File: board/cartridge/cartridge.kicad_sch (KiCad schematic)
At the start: 33 parts, among them J1 TF-115-BCP9, J2 HC-TYPE-C-16P-01B, J3 TC2030-NL, P1 Card Edge, SW1 K3-1410S, SW2 K3-1410S, U1 STM32G0B0RETx, U2 NAU8814Y, U3 AMS1117-3.3, Y1 X322516MLB4SI

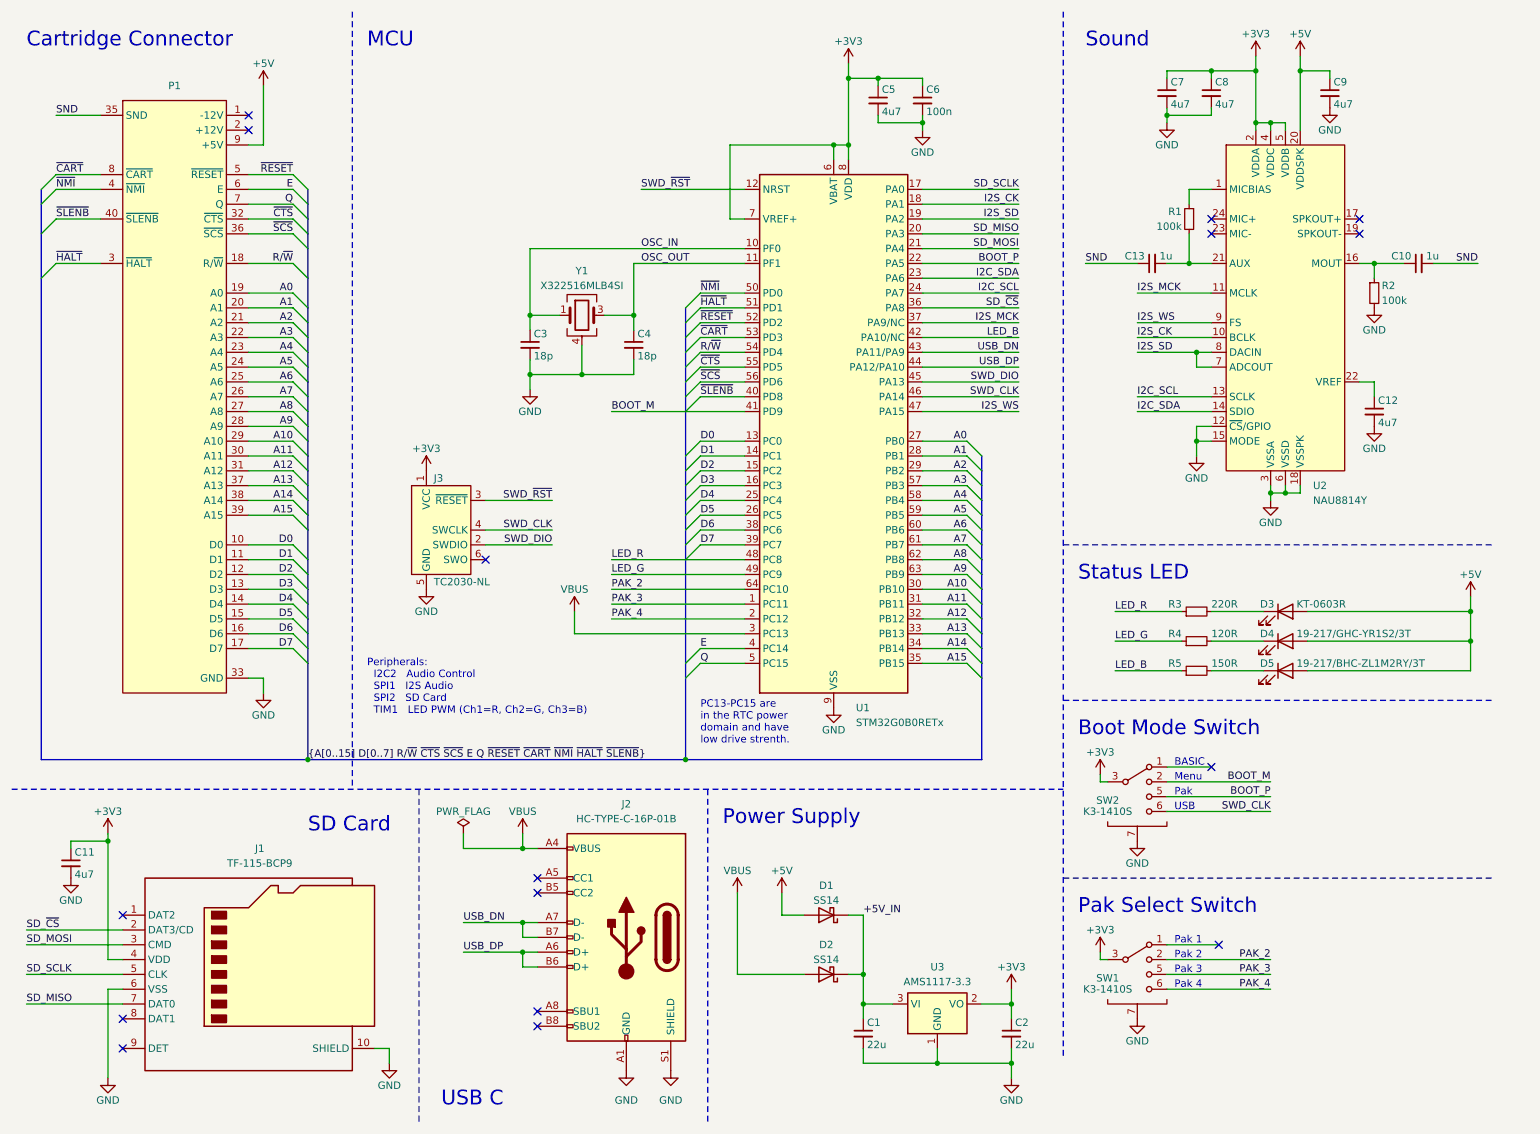
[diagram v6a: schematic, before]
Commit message: Update KiCad projects to v8.
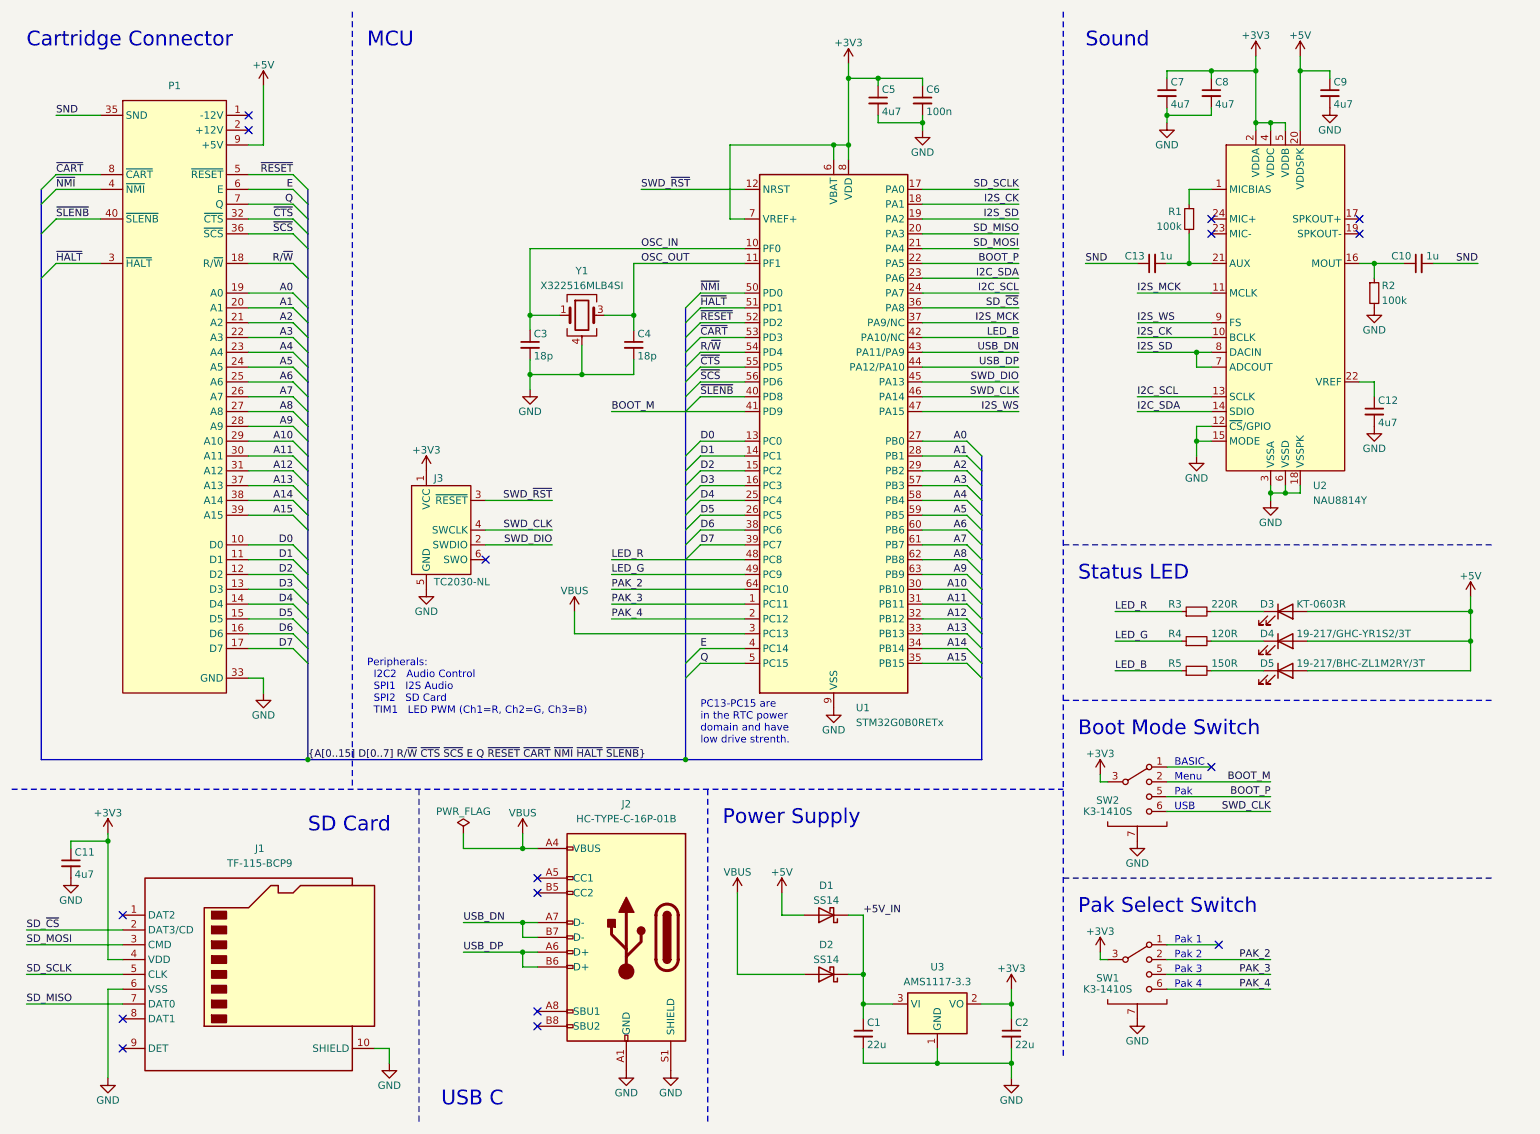
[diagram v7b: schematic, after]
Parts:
- J2: symbol Connector:USB_C_Receptacle_USB2.0 -> Connector:USB_C_Receptacle_USB2.0_16P

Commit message: Sketch out a redesign to use an RP2040.
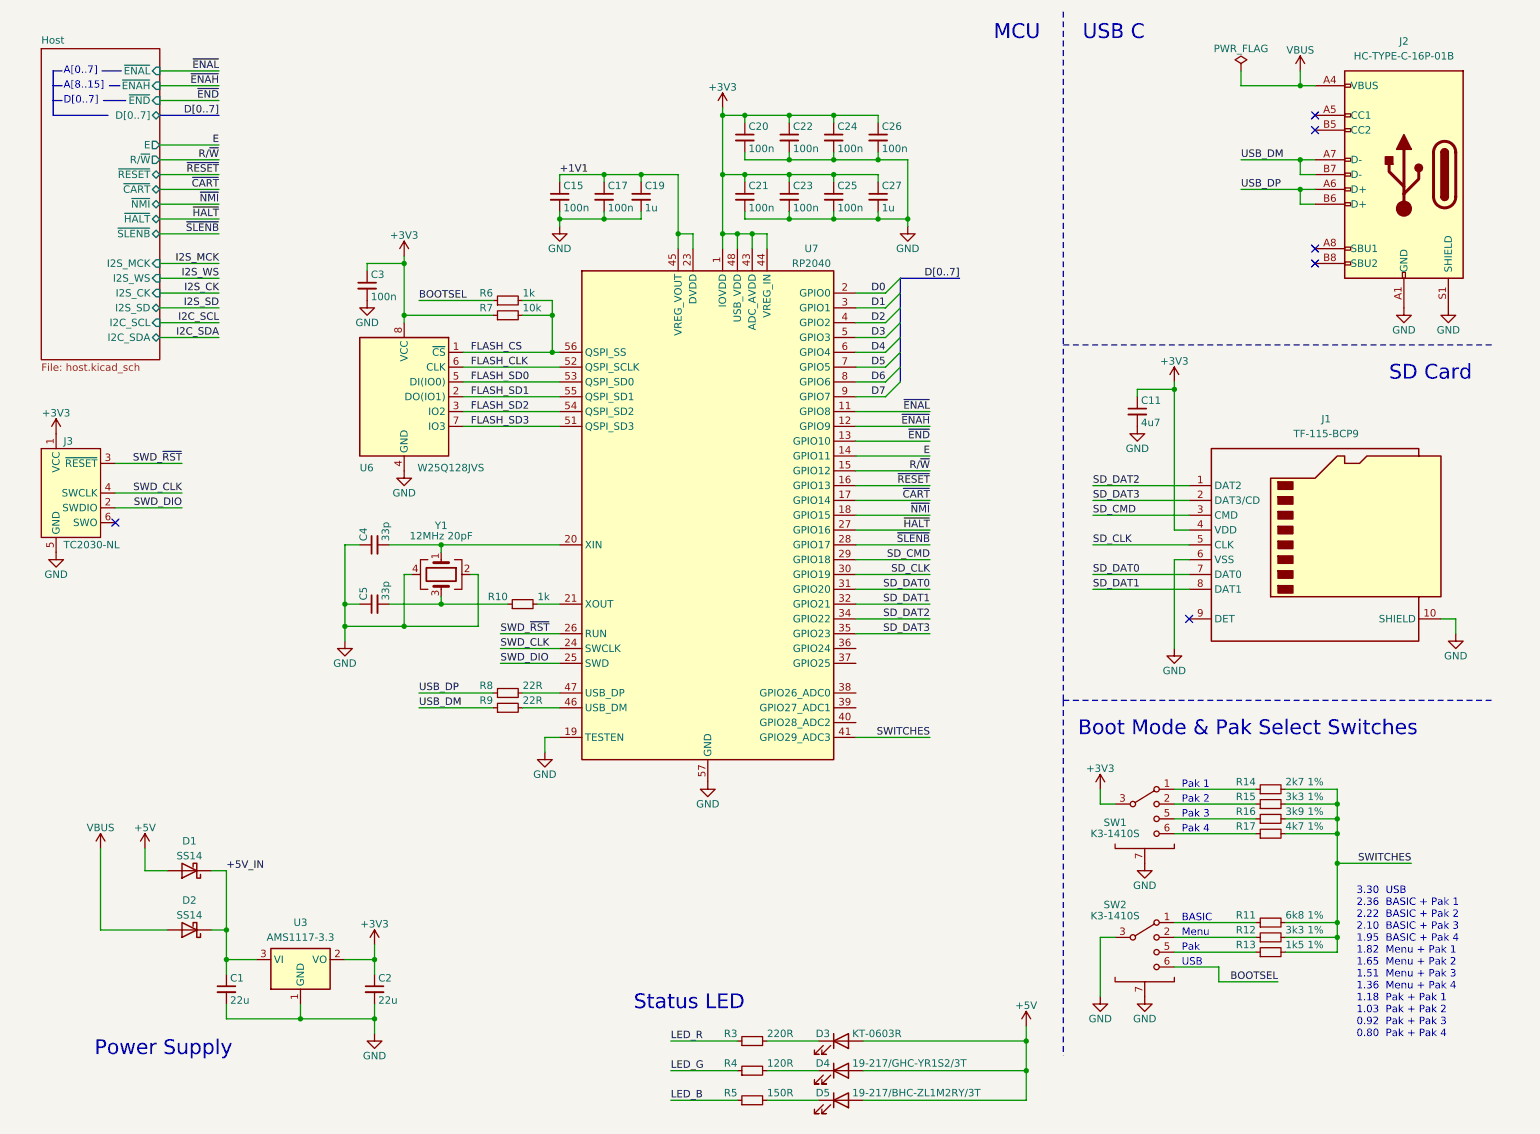
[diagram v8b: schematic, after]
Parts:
- removed C10, C13: 1u, Capacitor_SMD:C_0603_1608Metric, symbol Device:C_Small
- removed C12, C7, C8, C9: 4u7, Capacitor_SMD:C_0603_1608Metric, symbol Device:C_Small
- removed C6: 100n, Capacitor_SMD:C_0603_1608Metric, symbol Device:C_Small
- removed P1: Card Edge, 0Project:CoCo_Cart, symbol 0Project:CoCo_Cart
- removed R1, R2: 100k, Resistor_SMD:R_0603_1608Metric, symbol Device:R_Small
- removed U1: STM32G0B0RETx, Package_QFP:LQFP-64_10x10mm_P0.5mm, symbol MCU_ST_STM32G0:STM32G0B0RETx
- removed U2: NAU8814Y, Package_DFN_QFN:VQFN-24-1EP_4x4mm_P0.5mm_EP2.5x2.5mm, symbol 0Project:Nuvoton_NAU8814Y
- added C15, C17, C20, C21, C22, C23, C24, C25, C26: 100n, Capacitor_SMD:C_0603_1608Metric, symbol Device:C_Small
- added C19, C27: 1u, Capacitor_SMD:C_0603_1608Metric, symbol Device:C_Small
- added R10, R6: 1k, Resistor_SMD:R_0603_1608Metric, symbol Device:R_Small
- added R11: 6k8 1%, Resistor_SMD:R_0603_1608Metric, symbol Device:R_Small
- added R12, R15: 3k3 1%, Resistor_SMD:R_0603_1608Metric, symbol Device:R_Small
- added R13: 1k5 1%, Resistor_SMD:R_0603_1608Metric, symbol Device:R_Small
- added R14: 2k7 1%, Resistor_SMD:R_0603_1608Metric, symbol Device:R_Small
- added R16: 3k9 1%, Resistor_SMD:R_0603_1608Metric, symbol Device:R_Small
- added R17: 4k7 1%, Resistor_SMD:R_0603_1608Metric, symbol Device:R_Small
- added R7: 10k, Resistor_SMD:R_0603_1608Metric, symbol Device:R_Small
- added R8, R9: 22R, Resistor_SMD:R_0603_1608Metric, symbol Device:R_Small
- added U6: W25Q128JVS, Package_SO:SOIC-8_5.23x5.23mm_P1.27mm, symbol Memory_Flash:W25Q128JVS
- added U7: RP2040, Package_DFN_QFN:QFN-56-1EP_7x7mm_P0.4mm_EP3.2x3.2mm, symbol 0Project:RP2040
- C3: value 18p -> 100n
- C4: value 18p -> 33p
- C5: value 4u7 -> 33p
- Y1: value X322516MLB4SI -> 12MHz 20pF; LCSC C13738 -> C9002
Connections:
- net +3V3: now also C3.1, C20.1, C21.1, C22.1, C23.1, C24.1, C25.1, C26.1, C27.1, R7.1, U6.8 (VCC), U7.1 (IOVDD), U7.10 (IOVDD), U7.22 (IOVDD), U7.33 (IOVDD), U7.42 (IOVDD), U7.43 (ADC_AVDD), U7.44 (VREG_IN), U7.48 (USB_VDD), U7.49 (IOVDD); no longer C5.1, SW2.3 (COM), SW2.4 (COM)
- net D0: now also U7.2 (GPIO0)
- net D1: now also U7.3 (GPIO1)
- net D2: now also U7.4 (GPIO2)
- net D3: now also U7.5 (GPIO3)
- net D4: now also U7.6 (GPIO4)
- net D5: now also U7.7 (GPIO5)
- net D6: now also U7.8 (GPIO6)
- net D7: now also U7.9 (GPIO7)
- net E: now also U7.14 (GPIO11)
- net GND: now also C4.1, C5.1, SW2.3 (COM), SW2.4 (COM), C15.2, C17.2, C19.2, C20.2, C21.2, C22.2, C23.2, C24.2, C25.2, C26.2, C27.2, U6.4 (GND), U7.19 (TESTEN), U7.57 (GND); no longer C4.2, C5.2
- net R/~{W}: now also U7.15 (GPIO12)
- net SWD_CLK: now also U7.24 (SWCLK); no longer SW2.6 (4)
- net SWD_DIO: now also U7.25 (SWD)
- net SWD_~{RST}: now also U7.26 (RUN)
- net USB_DP: now also R8.1
- net ~{CART}: now also U7.17 (GPIO14)
- net ~{HALT}: now also U7.27 (GPIO16)
- net ~{NMI}: now also U7.18 (GPIO15)
- net ~{RESET}: now also U7.16 (GPIO13)
- net ~{SLENB}: now also U7.28 (GPIO17)
- net at SW1.1: now also R14.1
- net at SW2.1: now also R11.1
- net SD_DAT2: now reaches J1.1 (DAT2)
- net SD_DAT2: now also U7.34 (GPIO22)
- net SD_DAT1: now reaches J1.8 (DAT1)
- net SD_DAT1: now also U7.32 (GPIO21)
- net BOOT_M: no longer names the net of SW2.2
- net BOOT_M: now also R12.1
- net BOOT_P: no longer names the net of SW2.5 (3)
- net BOOT_P: now also R13.1
- net OSC_IN: no longer names the net of Y1.1
- net OSC_IN: now also C4.2, U7.20 (XIN); no longer C3.1
- net OSC_OUT: no longer names the net of Y1.3
- net OSC_OUT: now also C5.2, R10.1; no longer C4.1
- net PAK_2: no longer names the net of SW1.2
- net PAK_2: now also R15.1
- net PAK_3: no longer names the net of SW1.5 (3)
- net PAK_3: now also R16.1
- net PAK_4: no longer names the net of SW1.6 (4)
- net PAK_4: now also R17.1
- net SD_MISO renamed SD_DAT0
- net SD_DAT0: now also U7.31 (GPIO20)
- net SD_MOSI renamed SD_CMD
- net SD_CMD: now also U7.29 (GPIO18)
- net SD_SCLK renamed SD_CLK
- net SD_CLK: now also U7.30 (GPIO19)
- net SD_~{CS} renamed SD_DAT3
- net SD_DAT3: now also U7.35 (GPIO23)
- net USB_DN renamed USB_DM
- net USB_DM: now also R9.1
- new net: R10.2, U7.21 (XOUT)
- new net: R9.2, U7.46 (USB_DM)
- new net: R8.2, U7.47 (USB_DP)
- new net +1V1: C15.1, C17.1, C19.1, U7.23 (DVDD), U7.45 (VREG_VOUT), U7.50 (DVDD)
- new net BOOTSEL: R6.1, SW2.6 (4)
- new net FLASH_CLK: U6.6 (CLK), U7.52 (QSPI_SCLK)
- new net FLASH_CS: R6.2, R7.2, U6.1 (~{CS}), U7.56 (QSPI_SS)
- new net FLASH_SD0: U6.5 (DI(IO0)), U7.53 (QSPI_SD0)
- new net FLASH_SD1: U6.2 (DO(IO1)), U7.55 (QSPI_SD1)
- new net FLASH_SD2: U6.3 (IO2), U7.54 (QSPI_SD2)
- new net FLASH_SD3: U6.7 (IO3), U7.51 (QSPI_SD3)
- new net SWITCHES: R11.2, R12.2, R13.2, R14.2, R15.2, R16.2, R17.2, U7.41 (GPIO29_ADC3)
- new net ~{ENAH}: U7.12 (GPIO9)
- new net ~{ENAL}: U7.11 (GPIO8)
- new net ~{END}: U7.13 (GPIO10)
- no-connect marks 16 -> 6
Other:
- added sheet Host (host.kicad_sch)
- note added: "3.30 USB 2.36 BASIC + Pak 1 2.22 BASIC + Pak 2 2.10 BASIC + Pak 3 1.95 BASIC + Pak 4 1.82 Menu + Pak 1 1.65 Menu + Pak 2 1.51 Menu + Pak 3 1.36 Menu + Pak 4 1.18 Pak + Pak 1 1.03 Pak + Pak 2 0.92 Pak + Pak 3 0.80 Pak + Pak 4"
- note added: "A[0..7]"
- note added: "A[8..15]"
- note added: "Boot Mode & Pak Select Switches"
- note added: "D[0..7]"
- note removed: "Boot Mode Switch"
- note removed: "Cartridge Connector"
- note removed: "PC13-PC15 are in the RTC power domain and have low drive strenth."
- note removed: "Pak Select Switch"
- note removed: "Peripherals: I2C2 Audio Control SPI1 I2S Audio SPI2 SD Card TIM1 LED PWM (Ch1=R, Ch2=G, Ch3=B)"
- note removed: "Sound"
- company: © 2023 Sam Hanes, licensed under CERN-OHL-W v2 -> © 2023 Sam Hanes, licensed CERN-OHL-W v2
- title: CoCo Chameleon - Cartridge Emulator -> CoCo Chameleon Cartridge Emulator
- moved on the sheet: C1, C11, C2, D1, D2, D3, D4, D5, J1, J2, R3, R4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
